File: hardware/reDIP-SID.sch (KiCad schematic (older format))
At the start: 58 parts, among them J1 Conn_01x04, J2 Conn_01x04, J3 Conn_01x10, J4 Conn_01x10, J5 TYPE-C-31-M-12, J6 Conn_02x05_Odd_Even, SW1 KXT331LHS, U1 NCP115AMX120TCG, U2 NCP167AMX330TBG, U3 SN74CBTD16211DGVR, U4 SGTL5000XNLA3, U5 NUF2042XV6, U6 APS6404L-3SQR-SN, U7 W25Q128JVPIM, U8 ICE40UP5K-SG48I, X1 ECS-1612MV-240-CN-TR

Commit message: Revision 1.0
The board has been revised to remedy a few shortcomings on the first prototype:

* Added a separate LDO for the SGTL5000 VDDD, to keep the iCE40 VCC at 1.2V.
* Added DC bias for AUDIO_OUT, required by the C64 audio output stage.
* Increased board length by 2.54mm, facilitating some notable enhancements:
  - Symmetric stereo input (EXT_IN and EXT_IN_R). Note: External AC coupling.
  - Symmetric stereo output (AOUT_L and AOUT_R) in addition to AUDIO_OUT.
  - USB receptacle flush with board edge.
  - Fully 6581 / 8580 pin compatible.

Big thanks go to @smunaut, who has not only implemented support for the
reDIP SID in his [no2bootloader](https://github.com/no2fpga/no2bootloader),
but has also provided invaluable feedback from his testing of prototypes.
He pointed out that the internal SGTL5000 voltage regulator forced the
1.2V rail up to unsafe levels for the iCE40, and that DC bias is required
to drive the C64 audio output stage. He also suggested to add symmetric
stereo output, in addition to the SID audio output.
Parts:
- removed C10, C15, C8: 1uF, Capacitor_SMD:C_0201_0603Metric, symbol Device:C_Small
- removed J2: Conn_01x04, reDIP:PinHeader_1x04_P2.54mm_Vertical_LongTail, symbol Connector_Generic:Conn_01x04
- removed J4: Conn_01x10, reDIP:PinHeader_1x10_P2.54mm_Vertical, symbol Connector_Generic:Conn_01x10
- added C11: 1uF, Capacitor_SMD:C_0603_1608Metric, symbol Device:C_Small
- added C13: 10uF, Capacitor_SMD:C_0603_1608Metric, symbol Device:CP1_Small
- added C23, C7: 0.1uF, Capacitor_SMD:C_0201_0603Metric, symbol Device:C_Small
- added C5, C6: 1uF, Capacitor_SMD:C_0201_0603Metric, symbol Device:C_Small
- added J1: Conn_01x01, reDIP:PinHeader_1x01_P2.54mm_Vertical, symbol Connector_Generic:Conn_01x01
- added J3: Conn_01x14, reDIP:PinHeader_1x14_P2.54mm_Vertical, symbol Connector_Generic:Conn_01x14
- added R3, R5: 10k, Resistor_SMD:R_0201_0603Metric, symbol Device:R
- added TP2: TestPoint_Flag, reDIP:TestPoint_Pad_D0.75mm, symbol Connector:TestPoint_Flag
- added U3: NCP115AMX120TCG, ONSemi:CASE_711AJ_1.0x1.0mm_P0.65mm, symbol ONSemi:NCP115AMX120TCG
- added U7: MCP6H01T-E/OT, reDIP:SOT-23-5, symbol reDIP:Opamp_Inverting_SOT-23-5
- C10: renamed from C7; Notes 1.55V DC VAG DERATED TO 0.1uF -> 1.65V DC VAG DERATED TO 0.1uF
- C12: renamed from C9; value 1uF -> 10uF; footprint Capacitor_SMD:C_0201_0603Metric -> Capacitor_SMD:C_0603_1608Metric; symbol Device:C_Small -> Device:CP1_Small; Description CAP CER 1uF 6.3V 20% X6S 0201 -> CAP TANT 10uF 6.3V 20% 0603; Mfg Murata -> Vishay; Notes 1.55V DC AUDIO -> 1.65V DC 1.5V AC AUDIO; PN GRM033C80J105ME05D -> TMCJ0J106MTRF
- J2: renamed from J1; value Conn_01x04 -> Conn_01x05; footprint reDIP:PinHeader_1x04_P2.54mm_Vertical_LongTail -> reDIP:PinHeader_1x05_P2.54mm_Vertical; symbol Connector_Generic:Conn_01x04 -> Connector_Generic:Conn_01x05; Description CONN HEADER 4 POS .100\" SGL GOLD MATING 5.84mm TAIL 8.13mm -> CONN HEADER 5 POS .100\" SGL GOLD MATING 5.84mm TAIL 3.05mm; PN PRPC004SACN-RC -> PRPC005SAAN-RC
- U8: renamed from U6; value APS6404L-3SQR-SN -> LY68L6400SLIT; Mfg AP Memory -> Lyontek; Notes REPLACEMENT PARTS: Lyontek LY68L6400SLIT, Espressif ESP-PSR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 -> REPLACEMENT PARTS: AP Memory APS6404L-3SQR-SN, Espressif ES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; PN APS6404L-3SQR-SN -> LY68L6400SLIT
- X1: value ECS-1612MV-240-CN-TR -> ASCO-24.000MHZ-EK-T3; symbol ECS:ECS-1612MV-240-CN-TR -> Abracon:ASCO; Description OSC 24 MHz 25 ppm 1.6x1.2 mm -> OSC 24 MHz 30 ppm 1.6x1.2 mm; Mfg ECS -> Abracon; Notes (none) -> REPLACEMENT PARTS: ECS ECS-1612MV-240-CN-TR; PN ECS-1612MV-240-CN-TR -> ASCO-24.000MHZ-EK-T3
- renumbered C11 to C14, C12 to C15, C13 to C16, C14 to C17, C16 to C18, C17 to C19, C18 to C20, C19 to C21, C20 to C22, C5 to C8, C6 to C9, J3 to J4, R8 to R10, R9 to R11, R10 to R12, R11 to R13, R12 to R14, R13 to R15, R14 to R16, R3 to R4, R4 to R6, R5 to R7, R6 to R8, R7 to R9, TP2 to TP3, TP3 to TP4, U8 to U10, U3 to U4, U4 to U5, U5 to U6, U7 to U9
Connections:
- net labels added: AOUT_L, AOUT_R, EXT_IN_R, VDD, VDDD
- net labels removed: AUDIO_OUT_2
- wire segments 359 -> 394
- no-connect marks 17 -> 14
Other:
- note removed: "Decoupling\nshared with\nICE40 VCC"
- note removed: "Decoupling\nshared with\nSGTL5000\nVDDIO"
- moved on the sheet: C1, C10, C18, C19, C2, C3, C4, C8, C9, D1, D2, JP1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

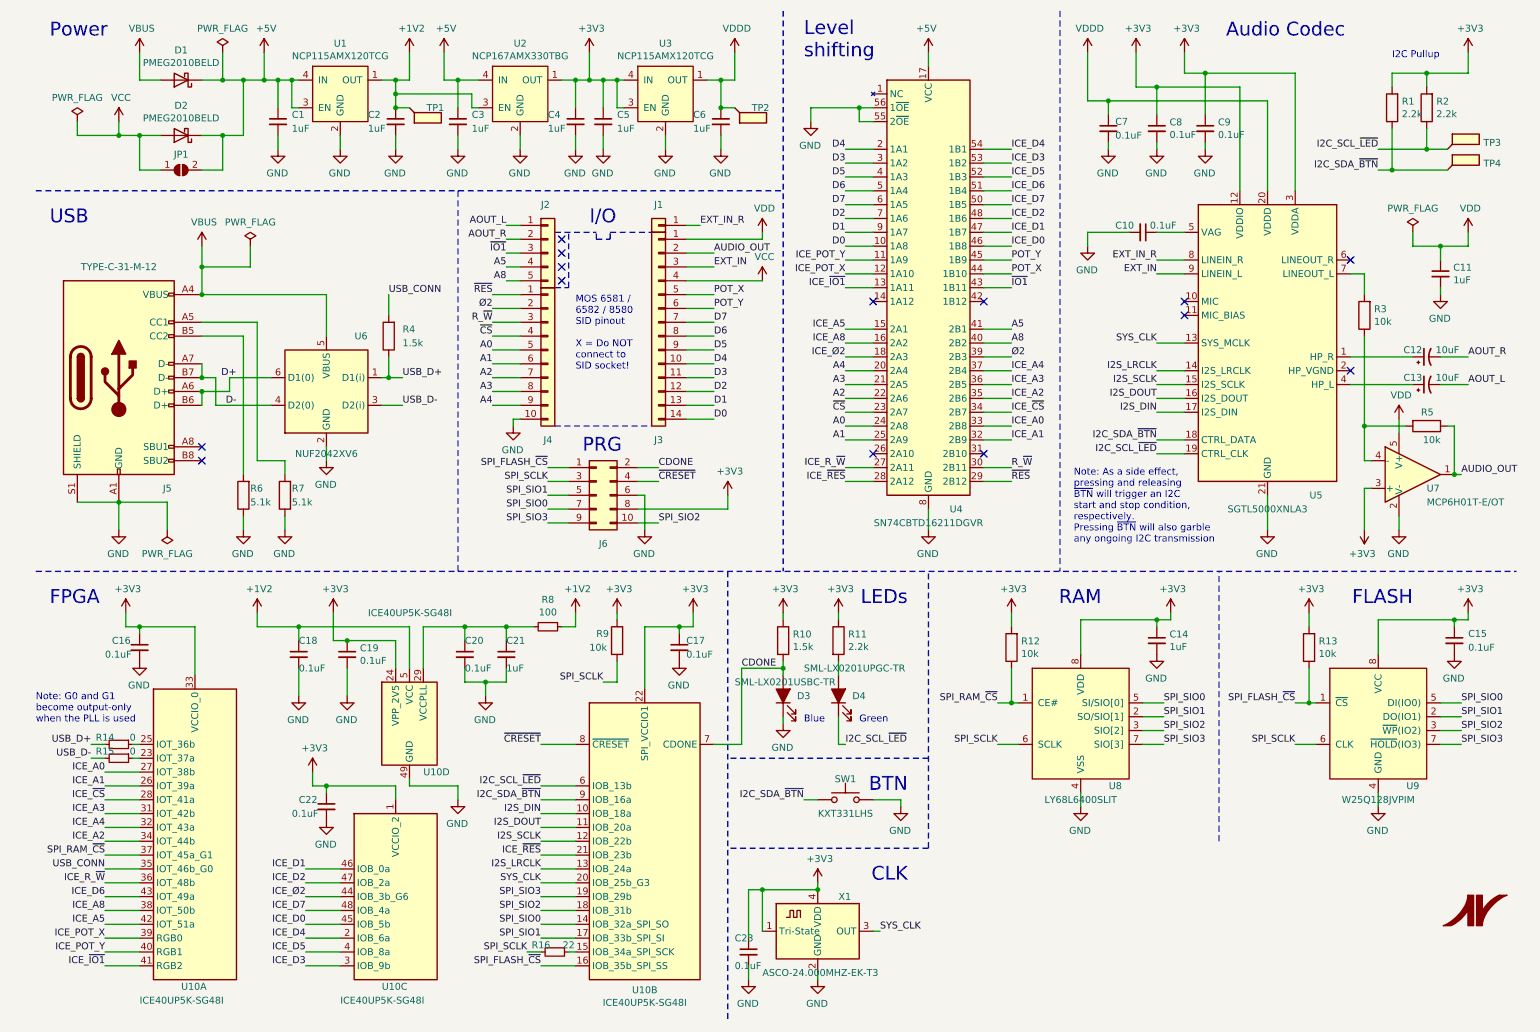
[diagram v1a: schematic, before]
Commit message: Hardware mixing of left and right channels to AUDIO_OUT
As suggested by @smunaut.
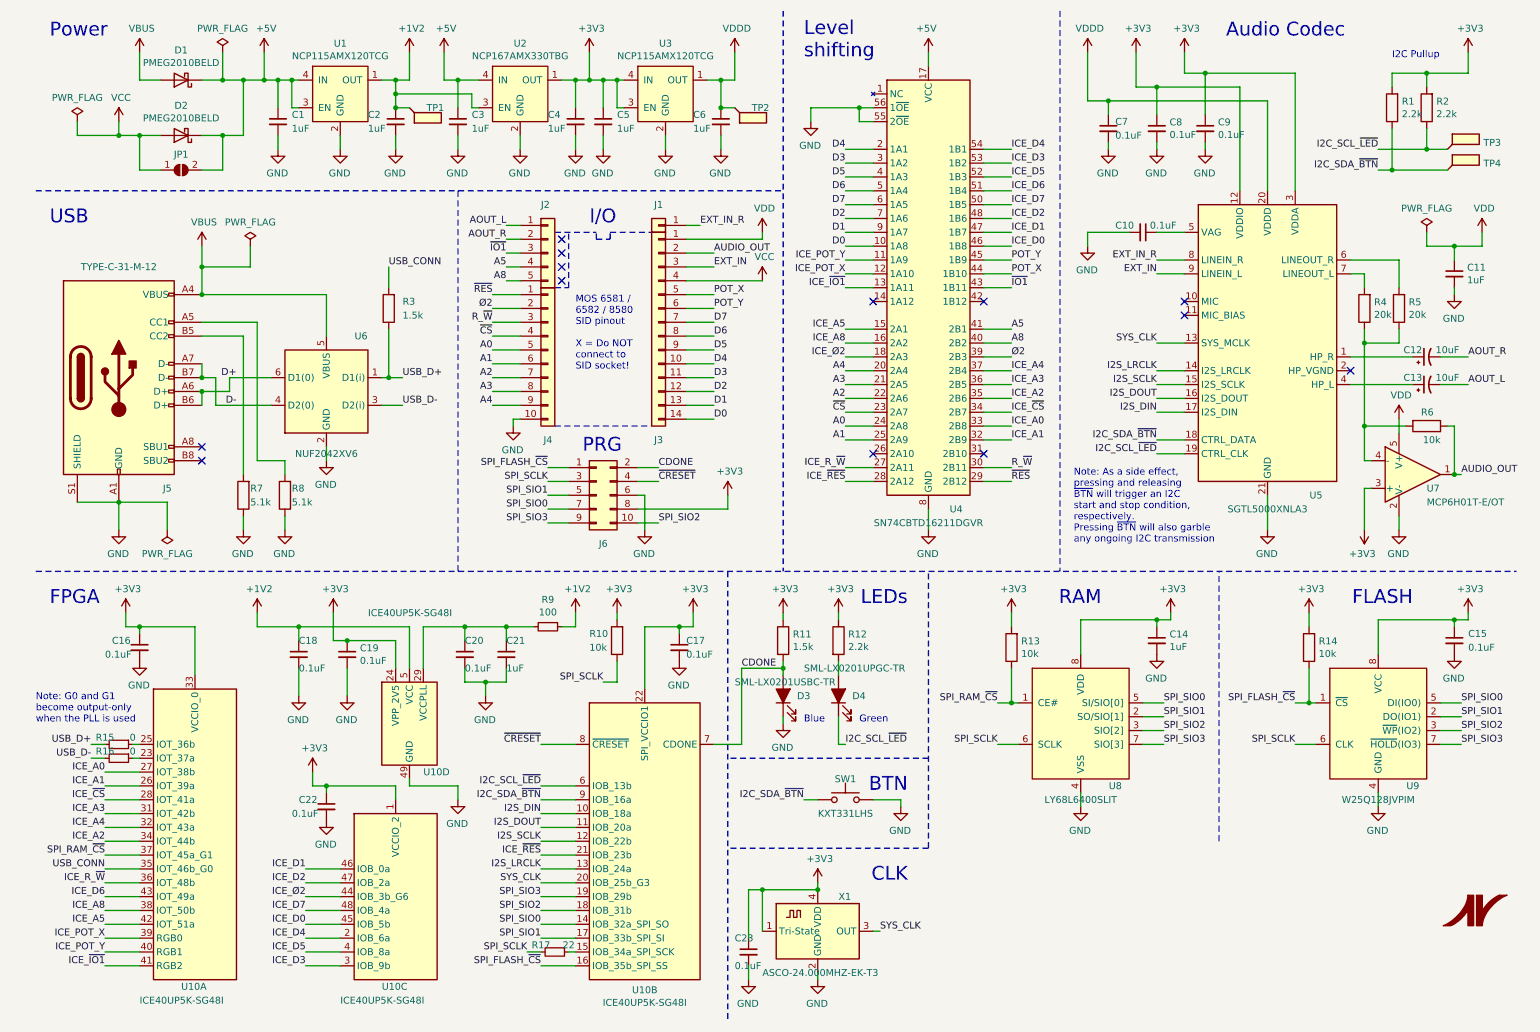
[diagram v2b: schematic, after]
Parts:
- added R5: 20k, Resistor_SMD:R_0201_0603Metric, symbol Device:R
- R4: renamed from R3; value 10k -> 20k; Description RES 10kΩ 50mW 1% 0201 -> RES 20kΩ 50mW 1% 0201; PN ERJ-1GNF1002C -> ERJ-1GNF2002C
- renumbered R9 to R10, R10 to R11, R11 to R12, R12 to R13, R13 to R14, R14 to R15, R15 to R16, R16 to R17, R4 to R3, R5 to R6, R6 to R7, R7 to R8, R8 to R9
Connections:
- net at U5.6 (LINEOUT_R): now also R5.2
- net at R4.1, R6.2, U7.4 (-): now also R5.1
- no-connect marks 14 -> 13
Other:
- moved on the sheet: C11, R3, R4
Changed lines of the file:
@@
 	7550 5500 7600 5500
 $Comp
-L Device:R R12
+L Device:R R13
 U 1 1 5F83658A
 P 7550 5100
-F 0 "R12" H 7480 5054 50  0000 R CNN
+F 0 "R13" H 7480 5054 50  0000 R CNN
 F 1 "10k" H 7480 5145 50  0000 R CNN
 F 2 "Resistor_SMD:R_0201_0603Metric" V 7480 5100 50  0001 C CNN
@@
 	9700 5500 9750 5500
 $Comp
-L Device:R R13
+L Device:R R14
 U 1 1 604FA973
 P 9700 5100
-F 0 "R13" H 9630 5054 50  0000 R CNN
+F 0 "R14" H 9630 5054 50  0000 R CNN
 F 1 "10k" H 9630 5145 50  0000 R CNN
 F 2 "Resistor_SMD:R_0201_0603Metric" V 9630 5100 50  0001 C CNN
@@
 $EndComp
 $Comp
-L Device:R_Small R8
+L Device:R_Small R9
 U 1 1 5E71845D
 P 4200 4950
-F 0 "R8" V 4004 4950 50  0000 C CNN
+F 0 "R9" V 4004 4950 50  0000 C CNN
 F 1 "100" V 4095 4950 50  0000 C CNN
 F 2 "Resistor_SMD:R_0201_0603Metric" H 4200 4950 50  0001 C CNN
@@
 	5900 5200 5900 5250
 $Comp
-L Device:R R10
+L Device:R R11
 U 1 1 5FE8D4E7
 P 5900 5050
-F 0 "R10" H 5970 5096 50  0000 L CNN
+F 0 "R11" H 5970 5096 50  0000 L CNN
 F 1 "1.5k" H 5970 5005 50  0000 L CNN
 F 2 "Resistor_SMD:R_0201_0603Metric" V 5830 5050 50  0001 C CNN
@@
 	1700 3350 1700 3250
 $Comp
-L Device:R R6
+L Device:R R7
 U 1 1 5EFEF82B
 P 2000 4000
-F 0 "R6" H 1950 3950 50  0000 R CNN
+F 0 "R7" H 1950 3950 50  0000 R CNN
 F 1 "5.1k" H 1950 4050 50  0000 R CNN
 F 2 "Resistor_SMD:R_0201_0603Metric" V 1930 4000 50  0001 C CNN
@@
 $EndComp
 $Comp
-L Device:R R7
+L Device:R R8
 U 1 1 5EFEFD1C
 P 2300 4000
-F 0 "R7" H 2250 3950 50  0000 R CNN
+F 0 "R8" H 2250 3950 50  0000 R CNN
 F 1 "5.1k" H 2250 4050 50  0000 R CNN
 F 2 "Resistor_SMD:R_0201_0603Metric" V 2230 4000 50  0001 C CNN
@@
 	-1   0    0    -1
 $EndComp
-$Comp
-L Device:R R4
-U 1 1 609EBD8B
-P 3050 2850
-F 0 "R4" H 2950 2800 50  0000 R CNN
-F 1 "1.5k" H 2950 2900 50  0000 R CNN
-F 2 "Resistor_SMD:R_0201_0603Metric" V 2980 2850 50  0001 C CNN
-F 3 "https://industrial.panasonic.com/ww/products/pt/general-purpose-chip-resistors/models/ERJ1GNJ152C" H 3050 2850 50  0001 C CNN
-F 4 "Panasonic" H 3050 2850 50  0001 C CNN "Mfg"
-F 5 "ERJ-1GNJ152C" H 3050 2850 50  0001 C CNN "PN"
-F 6 "RES 1.5kΩ 50mW 5% 0201" H 3050 2850 50  0001 C CNN "Description"
-	1    3050 2850
-	-1   0    0    1
-$EndComp
 Wire Wire Line
 	2600 3650 2600 3750
@@
 	6950 900  6950 800
 $Comp
-L Device:R_Small R16
+L Device:R_Small R17
 U 1 1 601AD4FD
 P 4250 7300
-F 0 "R16" V 4200 7200 50  0000 C CNN
+F 0 "R17" V 4200 7200 50  0000 C CNN
 F 1 "22" V 4200 7400 50  0000 C CNN
 F 2 "Resistor_SMD:R_0201_0603Metric" H 4250 7300 50  0001 C CNN
@@
 	5600 5250 5900 5250
 $Comp
-L Device:R R11
+L Device:R R12
 U 1 1 6005DB26
 P 6300 5050
-F 0 "R11" H 6370 5096 50  0000 L CNN
+F 0 "R12" H 6370 5096 50  0000 L CNN
 F 1 "2.2k" H 6370 5005 50  0000 L CNN
 F 2 "Resistor_SMD:R_0201_0603Metric" V 6230 5050 50  0001 C CNN
@@
 $EndComp
 $Comp
-L Device:R R9
+L Device:R R10
 U 1 1 637D16D1
 P 4700 5050
-F 0 "R9" H 4850 5000 50  0000 R CNN
+F 0 "R10" H 4900 5000 50  0000 R CNN
 F 1 "10k" H 4900 5100 50  0000 R CNN
 F 2 "Resistor_SMD:R_0201_0603Metric" V 4630 5050 50  0001 C CNN
@@
 $EndComp
 $Comp
-L Device:R_Small R14
+L Device:R_Small R15
 U 1 1 608C7719
 P 1100 5800
-F 0 "R14" V 1050 5700 50  0000 C CNN
+F 0 "R15" V 1050 5700 50  0000 C CNN
 F 1 "0" V 1050 5900 50  0000 C CNN
 F 2 "Resistor_SMD:R_0201_0603Metric" H 1100 5800 50  0001 C CNN
@@
 $EndComp
 $Comp
-L Device:R_Small R15
+L Device:R_Small R16
 U 1 1 608F3749
 P 1100 5900
-F 0 "R15" V 1050 5800 50  0000 C CNN
+F 0 "R16" V 1050 5800 50  0000 C CNN
 F 1 "0" V 1050 6000 50  0000 C CNN
 F 2 "Resistor_SMD:R_0201_0603Metric" H 1100 5900 50  0001 C CNN
@@
 Text Label 3150 3150 0    50   ~ 0
 USB_D+
-Text Label 3050 2550 0    50   ~ 0
-USB_CONN
 Wire Wire Line
-	3050 3000 3050 3150
+	3050 2800 3050 3150
 Connection ~ 3050 3150
 Wire Wire Line
@@
 	1    0    0    -1
 $EndComp
-Wire Wire Line
-	3050 2700 3050 2550
 Text Label 1000 6700 2    50   ~ 0
 USB_CONN
@@
 	10750 3500 10750 3850
 $Comp
-L Device:R R5
+L Device:R R6
 U 1 1 61896C00
 P 10550 3500
-F 0 "R5" V 10450 3550 50  0000 R CNN
+F 0 "R6" V 10450 3550 50  0000 R CNN
 F 1 "10k" V 10650 3600 50  0000 R CNN
 F 2 "Resistor_SMD:R_0201_0603Metric" V 10480 3500 50  0001 C CNN
@@
 	-1   0    0    -1
 $EndComp
-NoConn ~ 10000 2300
 Wire Wire Line
 	8100 2100 8400 2100
@@
 $EndComp
 Wire Wire Line
-	10100 2850 10100 3500
+	10100 2800 10100 2900
 Wire Wire Line
 	10000 2400 10100 2400
 Wire Wire Line
-	10100 2400 10100 2550
-Wire Wire Line
-	10650 2300 10650 2200
+	10750 2300 10750 2200
 Wire Wire Line
-	10650 2550 10650 2500
+	10750 2550 10750 2500
 $Comp
 L power:GND #PWR031
 U 1 1 61311990
-P 10650 2550
-F 0 "#PWR031" H 10650 2300 50  0001 C CNN
-F 1 "GND" H 10655 2377 50  0000 C CNN
-F 2 "" H 10650 2550 50  0001 C CNN
-F 3 "" H 10650 2550 50  0001 C CNN
-	1    10650 2550
+P 10750 2550
+F 0 "#PWR031" H 10750 2300 50  0001 C CNN
+F 1 "GND" H 10755 2377 50  0000 C CNN
+F 2 "" H 10750 2550 50  0001 C CNN
+F 3 "" H 10750 2550 50  0001 C CNN
+	1    10750 2550
 	-1   0    0    -1
 $EndComp
@@
 L Device:C_Small C11
 U 1 1 6131199A
-P 10650 2400
-F 0 "C11" H 10742 2446 50  0000 L CNN
-F 1 "1uF" H 10742 2355 50  0000 L CNN
-F 2 "Capacitor_SMD:C_0603_1608Metric" H 10650 2400 50  0001 C CNN
-F 3 "https://www.murata.com/products/productdetail.aspx?partno=GRM188R61C475ME11D" H 10650 2400 50  0001 C CNN
-F 4 "Murata" H 10650 2400 50  0001 C CNN "Mfg"
-F 5 "GRM188R61C475ME11D" H 10650 2400 50  0001 C CNN "PN"
-F 6 "CAP CER 4.7uF 16V 20% X5R 0603" H 10650 2400 50  0001 C CNN "Description"
-F 7 "9V/12V DC DERATED TO 1uF" H 10650 2400 50  0001 C CNN "Notes"
-	1    10650 2400
+P 10750 2400
+F 0 "C11" H 10842 2446 50  0000 L CNN
+F 1 "1uF" H 10842 2355 50  0000 L CNN
+F 2 "Capacitor_SMD:C_0603_1608Metric" H 10750 2400 50  0001 C CNN
+F 3 "https://www.murata.com/products/productdetail.aspx?partno=GRM188R61C475ME11D" H 10750 2400 50  0001 C CNN
+F 4 "Murata" H 10750 2400 50  0001 C CNN "Mfg"
+F 5 "GRM188R61C475ME11D" H 10750 2400 50  0001 C CNN "PN"
+F 6 "CAP CER 4.7uF 16V 20% X5R 0603" H 10750 2400 50  0001 C CNN "Description"
+F 7 "9V/12V DC DERATED TO 1uF" H 10750 2400 50  0001 C CNN "Notes"
+	1    10750 2400
 	1    0    0    -1
 $EndComp
@@
 L power:VDD #PWR027
 U 1 1 6133E977
-P 10850 2100
-F 0 "#PWR027" H 10850 1950 50  0001 C CNN
-F 1 "VDD" H 10865 2273 50  0000 C CNN
-F 2 "" H 10850 2100 50  0001 C CNN
-F 3 "" H 10850 2100 50  0001 C CNN
-	1    10850 2100
+P 10950 2100
+F 0 "#PWR027" H 10950 1950 50  0001 C CNN
+F 1 "VDD" H 10965 2273 50  0000 C CNN
+F 2 "" H 10950 2100 50  0001 C CNN
+F 3 "" H 10950 2100 50  0001 C CNN
+	1    10950 2100
 	1    0    0    -1
 $EndComp
@@
 	4250 3500 4950 3500
 Wire Wire Line
-	10650 2200 10450 2200
+	10750 2200 10550 2200
 Wire Wire Line
-	10850 2200 10850 2100
+	10950 2200 10950 2100
 $Comp
 L power:PWR_FLAG #FLG03
 U 1 1 617C63A1
-P 10450 2100
-F 0 "#FLG03" H 10450 2175 50  0001 C CNN
-F 1 "PWR_FLAG" H 10450 2273 50  0000 C CNN
-F 2 "" H 10450 2100 50  0001 C CNN
-F 3 "~" H 10450 2100 50  0001 C CNN
-	1    10450 2100
+P 10550 2100
+F 0 "#FLG03" H 10550 2175 50  0001 C CNN
+F 1 "PWR_FLAG" H 10550 2273 50  0000 C CNN
+F 2 "" H 10550 2100 50  0001 C CNN
+F 3 "~" H 10550 2100 50  0001 C CNN
+	1    10550 2100
 	1    0    0    -1
 $EndComp
 Wire Wire Line
-	10850 2200 10650 2200
-Connection ~ 10650 2200
+	10950 2200 10750 2200
+Connection ~ 10750 2200
 Wire Wire Line
-	10450 2200 10450 2100
+	10550 2200 10550 2100
 $Comp
-L Device:R R3
+L Device:R R5
+U 1 1 61239312
+P 10350 2650
+F 0 "R5" H 10280 2604 50  0000 R CNN
+F 1 "20k" H 10280 2695 50  0000 R CNN
+F 2 "Resistor_SMD:R_0201_0603Metric" V 10280 2650 50  0001 C CNN
+F 3 "https://industrial.panasonic.com/ww/products/pt/general-purpose-chip-resistors/models/ERJ1GNF2002C" H 10350 2650 50  0001 C CNN
+F 4 "Panasonic" H 10350 2650 50  0001 C CNN "Mfg"
+F 5 "ERJ-1GNF2002C" H 10350 2650 50  0001 C CNN "PN"
+F 6 "RES 20kΩ 50mW 1% 0201" H 10350 2650 50  0001 C CNN "Description"
+	1    10350 2650
+	-1   0    0    1
+$EndComp
+Wire Wire Line
+	10100 2400 10100 2500
+$Comp
+L Device:R R4
 U 1 1 615D34A5
-P 10100 2700
-F 0 "R3" H 10030 2654 50  0000 R CNN
-F 1 "10k" H 10030 2745 50  0000 R CNN
-F 2 "Resistor_SMD:R_0201_0603Metric" V 10030 2700 50  0001 C CNN
-F 3 "https://industrial.panasonic.com/ww/products/pt/general-purpose-chip-resistors/models/ERJ1GNF1002C" H 10100 2700 50  0001 C CNN
-F 4 "Panasonic" H 10100 2700 50  0001 C CNN "Mfg"
-F 5 "ERJ-1GNF1002C" H 10100 2700 50  0001 C CNN "PN"
-F 6 "RES 10kΩ 50mW 1% 0201" H 10100 2700 50  0001 C CNN "Description"
-	1    10100 2700
+P 10100 2650
+F 0 "R4" H 10030 2604 50  0000 R CNN
+F 1 "20k" H 10030 2695 50  0000 R CNN
+F 2 "Resistor_SMD:R_0201_0603Metric" V 10030 2650 50  0001 C CNN
+F 3 "https://industrial.panasonic.com/ww/products/pt/general-purpose-chip-resistors/models/ERJ1GNF2002C" H 10100 2650 50  0001 C CNN
+F 4 "Panasonic" H 10100 2650 50  0001 C CNN "Mfg"
+F 5 "ERJ-1GNF2002C" H 10100 2650 50  0001 C CNN "PN"
+F 6 "RES 20kΩ 50mW 1% 0201" H 10100 2650 50  0001 C CNN "Description"
+	1    10100 2650
+	-1   0    0    1
+$EndComp
+Wire Wire Line
+	10350 2800 10350 2900
+Wire Wire Line
+	10350 2900 10100 2900
+Connection ~ 10100 2900
+Wire Wire Line
+	10100 2900 10100 3500
+Wire Wire Line
+	10350 2500 10350 2300
+Wire Wire Line
+	10350 2300 10000 2300
+$Comp
+L Device:R R3
+U 1 1 609EBD8B
+P 3050 2650
+F 0 "R3" H 2950 2600 50  0000 R CNN
+F 1 "1.5k" H 2950 2700 50  0000 R CNN
+F 2 "Resistor_SMD:R_0201_0603Metric" V 2980 2650 50  0001 C CNN
+F 3 "https://industrial.panasonic.com/ww/products/pt/general-purpose-chip-resistors/models/ERJ1GNJ152C" H 3050 2650 50  0001 C CNN
+F 4 "Panasonic" H 3050 2650 50  0001 C CNN "Mfg"
+F 5 "ERJ-1GNJ152C" H 3050 2650 50  0001 C CNN "PN"
+F 6 "RES 1.5kΩ 50mW 5% 0201" H 3050 2650 50  0001 C CNN "Description"
+	1    3050 2650
 	-1   0    0    1
 $EndComp
+Text Label 3050 2350 0    50   ~ 0
+USB_CONN
+Wire Wire Line
+	3050 2500 3050 2350
 $EndSCHEMATC
